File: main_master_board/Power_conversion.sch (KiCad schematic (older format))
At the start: 64 parts, among them IC1 IC_MCP73831, U10 FDS4935A, U11 Si1900DL, U12 FDS4935A, U2 LP3852-3.3, U20 TPS82084SIL, U3 TPS61232DRC, U4 LMR16030, U5 Si1900DL, U6 74AUC1G32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

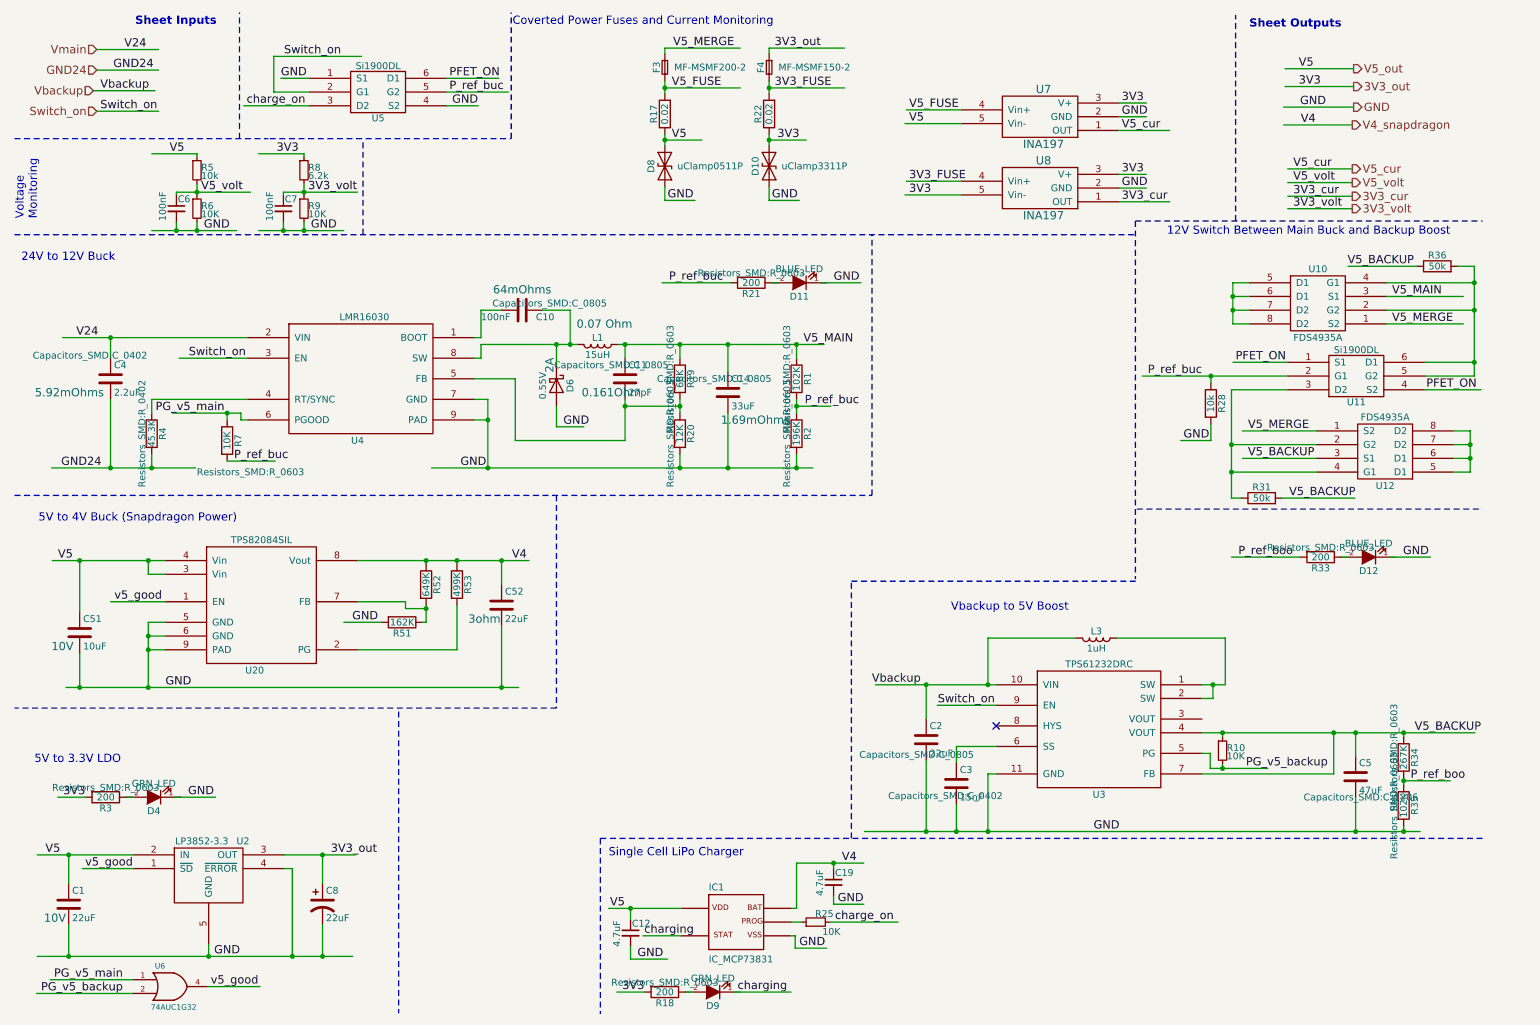
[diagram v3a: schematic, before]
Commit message: Cleaned up some wires and moved connectors out to main page. Also added some LEDs
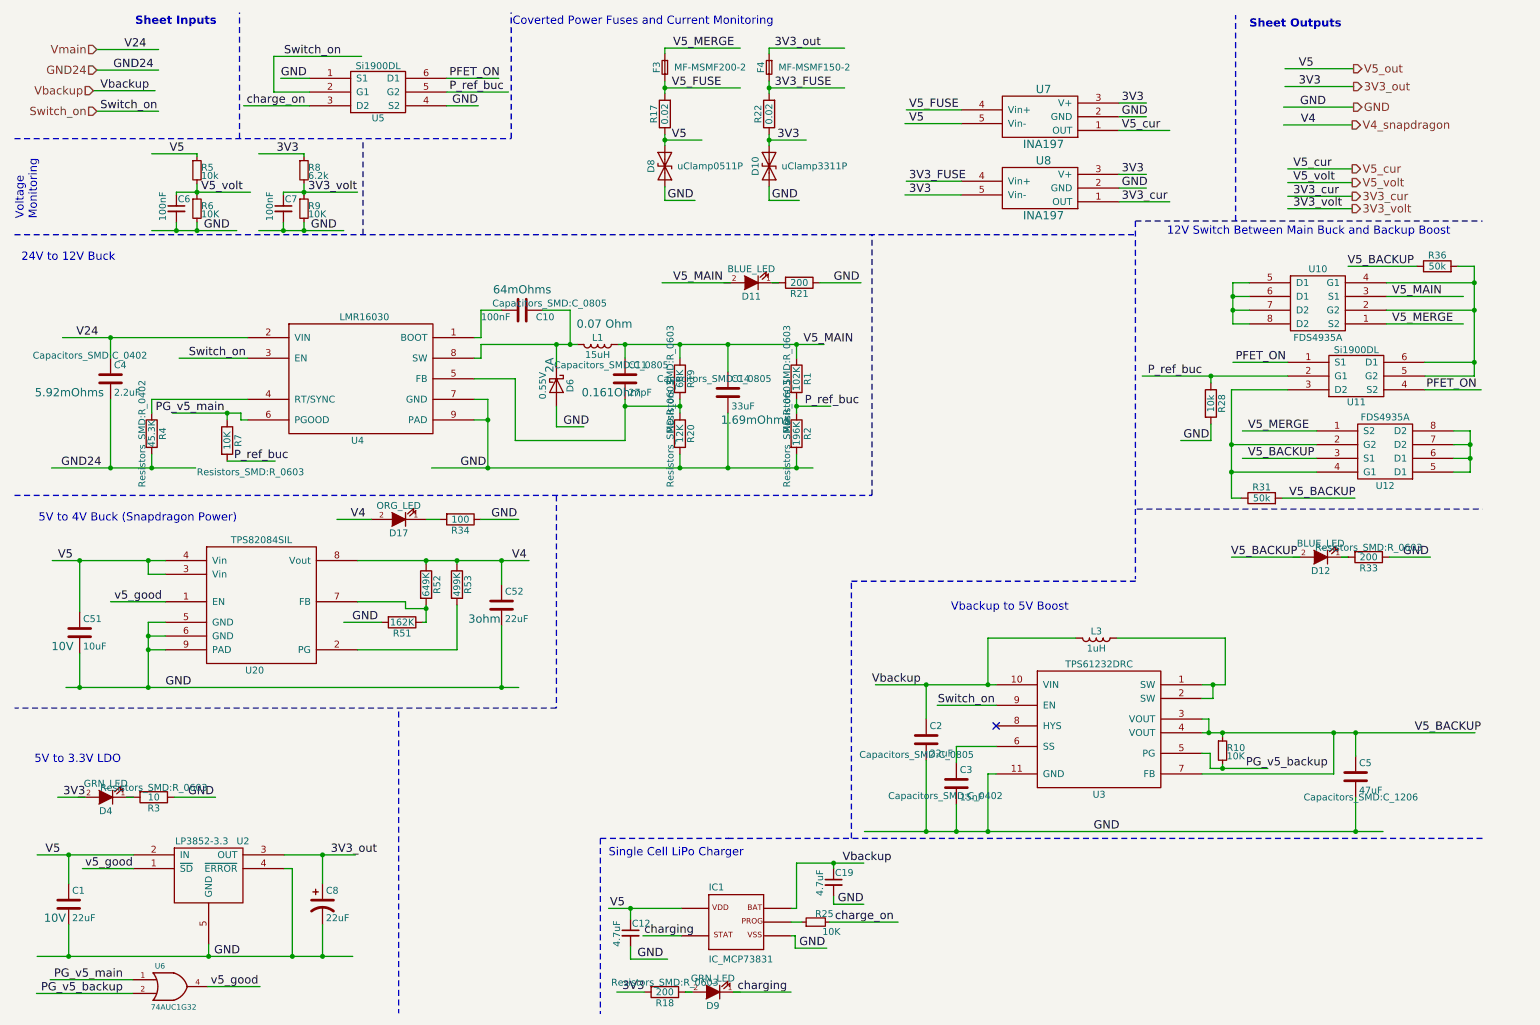
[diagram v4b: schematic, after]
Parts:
- removed R35: 102K, Resistors_SMD:R_0603, symbol R
- added D17: ORG_LED, LEDs:LED_0603, symbol LED
- R3: value 200 -> 10
- R34: value 267K -> 100
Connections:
- net labels removed: P_ref_boo
- wire segments 236 -> 237
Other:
- moved on the sheet: D11, D12, D4, R21, R3, R33
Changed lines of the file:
@@
 LIBS:Sensors
 LIBS:LP3852-3.3
-LIBS:decaWave
+LIBS:0s102011ma1qn1
+LIBS:74LVC1G17
+LIBS:74V1T126
+LIBS:acs711klctr-12ab-t
+LIBS:AD7192
+LIBS:AD7193
+LIBS:am-hrr30-xxx
+LIBS:aon7528
+LIBS:AP7363
+LIBS:AS1359
+LIBS:csd16323q3
+LIBS:dmn2004dmk
+LIBS:dp_devices
+LIBS:DSPIC33E128MC506
+LIBS:fds6898az
+LIBS:ina197
+LIBS:irf7329pbf
+LIBS:ld1117
+LIBS:lm3478
+LIBS:lm3481
+LIBS:lt1910
+LIBS:ltc1871
+LIBS:ltc1982
+LIBS:MAG3110
+LIBS:mcp1700
+LIBS:mcp73831
+LIBS:mcsmt-g5030a1-3712
+LIBS:microchip_can
+LIBS:microclasp_hdrx2
+LIBS:microclasp_hdrx3
+LIBS:MPU-6000_MPU-6050
+LIBS:MPU-9150
+LIBS:nrf24l01+
+LIBS:pds1040l
+LIBS:pic12f1571
+LIBS:pinhead
+LIBS:psmn013-80ys
+LIBS:RESISTOR_ARRAY
+LIBS:rf803d
+LIBS:RGB_LED
+LIBS:Si1970DH
+LIBS:sn65hvd232
+LIBS:ssc54
+LIBS:sw_push_4
+LIBS:tc74
+LIBS:TPS2113A
+LIBS:tps54540
+LIBS:vs-mbrb1635pbf
+LIBS:xal5050-562meb
+LIBS:xal6030-182mec
 LIBS:conn_2x50
 LIBS:conn_open_q_x2
@@
 LIBS:ac-dc
 LIBS:actel
-LIBS:allegro
 LIBS:Altera
 LIBS:analog_devices
@@
 LIBS:logo
 LIBS:maxim
-LIBS:mechanical
 LIBS:microchip_dspic33dsc
 LIBS:microchip_pic10mcu
@@
 LIBS:microchip_pic32mcu
 LIBS:motor_drivers
-LIBS:motors
 LIBS:msp430
 LIBS:nordicsemi
@@
 LIBS:ttl_ieee
 LIBS:video
-LIBS:wiznet
 LIBS:Worldsemi
 LIBS:Xicor
-LIBS:zetex
 LIBS:Zilog
 LIBS:conn_2x45
@@
 $Descr A4 11693 8268
 encoding utf-8
-Sheet 2 7
+Sheet 2 6
 Title ""
 Date ""
@@
 L R R33
 U 1 1 58669BFA
-P 10020 4450
-F 0 "R33" V 10100 4450 50  0000 C CNN
-F 1 "200" V 10020 4450 50  0000 C CNN
-F 2 "Resistors_SMD:R_0603" V 9950 4450 50  0000 C CNN
-F 3 "" H 10020 4450 50  0000 C CNN
-	1    10020 4450
+P 10370 4450
+F 0 "R33" V 10450 4450 50  0000 C CNN
+F 1 "200" V 10370 4450 50  0000 C CNN
+F 2 "Resistors_SMD:R_0603" V 10300 4450 50  0000 C CNN
+F 3 "" H 10370 4450 50  0000 C CNN
+	1    10370 4450
 	0    1    1    0
 $EndComp
@@
 L LED-RESCUE-main_master_board D?
 U 1 1 5866D243
-P 1515 6200
+P 1165 6200
 AR Path="/5866D243" Ref="D?"  Part="1"
 AR Path="/58643B62/5866D243" Ref="D4"  Part="1"
 AR Path="/5876FF98/5866D243" Ref="D4"  Part="1"
-F 0 "D4" H 1515 6300 50  0000 C CNN
-F 1 "GRN_LED" H 1515 6100 50  0000 C CNN
-F 2 "LEDs:LED_0603" H 1515 6200 50  0001 C CNN
-F 3 "http://www.digikey.com/product-detail/en/kingbright/APT1608ZGC/754-1126-1-ND" H 1515 6200 50  0001 C CNN
-	1    1515 6200
+F 0 "D4" H 1165 6300 50  0000 C CNN
+F 1 "GRN_LED" H 1165 6100 50  0000 C CNN
+F 2 "LEDs:LED_0603" H 1165 6200 50  0001 C CNN
+F 3 "http://www.digikey.com/product-detail/en/kingbright/APT1608ZGC/754-1126-1-ND" H 1165 6200 50  0001 C CNN
+	1    1165 6200
 	-1   0    0    1
 $EndComp
@@
 L R R3
 U 1 1 5866D24A
-P 1165 6200
-F 0 "R3" V 1245 6200 50  0000 C CNN
-F 1 "200" V 1165 6200 50  0000 C CNN
-F 2 "Resistors_SMD:R_0603" V 1095 6200 50  0000 C CNN
-F 3 "" H 1165 6200 50  0000 C CNN
-	1    1165 6200
+P 1515 6200
+F 0 "R3" V 1595 6200 50  0000 C CNN
+F 1 "10" V 1515 6200 50  0000 C CNN
+F 2 "Resistors_SMD:R_0603" V 1445 6200 50  0000 C CNN
+F 3 "" H 1515 6200 50  0000 C CNN
+	1    1515 6200
 	0    1    1    0
 $EndComp
@@
 Vbackup
 $Comp
-L R R34
-U 1 1 586BFF78
-P 10625 5910
-F 0 "R34" V 10705 5910 50  0000 C CNN
-F 1 "267K" V 10625 5910 50  0000 C CNN
-F 2 "Resistors_SMD:R_0603" V 10555 5910 50  0000 C CNN
-F 3 "" H 10625 5910 50  0000 C CNN
-	1    10625 5910
-	1    0    0    -1
-$EndComp
-$Comp
-L R R35
-U 1 1 586C095E
-P 10625 6260
-F 0 "R35" V 10705 6260 50  0000 C CNN
-F 1 "102K" V 10625 6260 50  0000 C CNN
-F 2 "Resistors_SMD:R_0603" V 10555 6260 50  0000 C CNN
-F 3 "" H 10625 6260 50  0000 C CNN
-	1    10625 6260
-	1    0    0    -1
-$EndComp
-Text Label 10675 6080 0    60   ~ 0
-P_ref_boo
-Text Label 9420 4450 0    60   ~ 0
-P_ref_boo
-$Comp
 L LED-RESCUE-main_master_board D11
 U 1 1 586C4FFA
-P 6220 2450
-F 0 "D11" H 6220 2550 50  0000 C CNN
-F 1 "BLUE_LED" H 6220 2350 50  0000 C CNN
-F 2 "LEDs:LED_0603" H 6220 2450 50  0001 C CNN
-F 3 "http://www.digikey.com/product-detail/en/vishay-semiconductor-opto-division/VLMB1310-GS08/VLMB1310-GS08CT-ND" H 6220 2450 50  0001 C CNN
-	1    6220 2450
+P 5870 2450
+F 0 "D11" H 5870 2550 50  0000 C CNN
+F 1 "BLUE_LED" H 5870 2350 50  0000 C CNN
+F 2 "LEDs:LED_0603" H 5870 2450 50  0001 C CNN
+F 3 "http://www.digikey.com/product-detail/en/vishay-semiconductor-opto-division/VLMB1310-GS08/VLMB1310-GS08CT-ND" H 5870 2450 50  0001 C CNN
+	1    5870 2450
 	-1   0    0    1
 $EndComp
@@
 L R R21
 U 1 1 586C5001
-P 5870 2450
-F 0 "R21" V 5950 2450 50  0000 C CNN
-F 1 "200" V 5870 2450 50  0000 C CNN
-F 2 "Resistors_SMD:R_0603" V 5800 2450 50  0000 C CNN
-F 3 "" H 5870 2450 50  0000 C CNN
-	1    5870 2450
+P 6220 2450
+F 0 "R21" V 6300 2450 50  0000 C CNN
+F 1 "200" V 6220 2450 50  0000 C CNN
+F 2 "Resistors_SMD:R_0603" V 6150 2450 50  0001 C CNN
+F 3 "" H 6220 2450 50  0000 C CNN
+	1    6220 2450
 	0    1    1    0
 $EndComp
-Text Label 5270 2450 0    60   ~ 0
-P_ref_buc
 Text Label 6260 3350 0    60   ~ 0
 P_ref_buc
@@
 L LED-RESCUE-main_master_board D12
 U 1 1 586C9705
-P 10370 4450
-F 0 "D12" H 10370 4550 50  0000 C CNN
-F 1 "BLUE_LED" H 10370 4350 50  0000 C CNN
-F 2 "LEDs:LED_0603" H 10370 4450 50  0001 C CNN
-F 3 "http://www.digikey.com/product-detail/en/vishay-semiconductor-opto-division/VLMB1310-GS08/VLMB1310-GS08CT-ND" H 10370 4450 50  0001 C CNN
-	1    10370 4450
+P 10020 4450
+F 0 "D12" H 10020 4550 50  0000 C CNN
+F 1 "BLUE_LED" H 10020 4350 50  0000 C CNN
+F 2 "LEDs:LED_0603" H 10020 4450 50  0001 C CNN
+F 3 "http://www.digikey.com/product-detail/en/vishay-semiconductor-opto-division/VLMB1310-GS08/VLMB1310-GS08CT-ND" H 10020 4450 50  0001 C CNN
+	1    10020 4450
 	-1   0    0    1
 $EndComp
@@
 Text Label 9400 3030 0    60   ~ 0
 PFET_ON
-Text Label 8760 3130 0    60   ~ 0
-P_ref_buc
 Text Label 9020 3600 0    60   ~ 0
 GND
@@
 Text Label 6500 6980 0    60   ~ 0
 GND
-Text Label 6530 6680 0    60   ~ 0
-V4
 Text Notes 4830 6640 0    60   ~ 0
 Single Cell LiPo Charger
@@
 	11200 6500 5700 6500
 Wire Wire Line
-	10625 6060 10625 6110
-Wire Wire Line
-	10625 6080 10965 6080
-Connection ~ 10625 6080
-Wire Wire Line
 	5220 2450 5720 2450
 Wire Wire Line
@@
 	10260 1170 9750 1170
 Wire Wire Line
-	6695 6450 10745 6450
+	6695 6450 10475 6450
 Wire Wire Line
 	7655 6030 7595 6030
@@
 Connection ~ 10115 5730
 Wire Wire Line
-	10275 6200 10275 6450
+	10275 6450 10275 6200
 Connection ~ 10275 6450
 Wire Wire Line
@@
 Switch_on
 NoConn ~ 7655 5680
-Wire Wire Line
-	10625 5760 10625 5730
-Connection ~ 10625 5730
-Wire Wire Line
-	10625 6410 10625 6450
-Connection ~ 10625 6450
 Text Label 10705 5730 0    60   ~ 0
 V5_BACKUP
@@
 Text Label 9875 1300 0    60   ~ 0
 V4
+Text Label 5300 2450 0    60   ~ 0
+V5_MAIN
+Text Label 9850 4450 2    60   ~ 0
+V5_BACKUP
+Text Label 6535 6680 0    60   ~ 0
+Vbackup
+$Comp
+L LED D17
+U 1 1 588AAACC
+P 3300 4175
+F 0 "D17" H 3300 4275 50  0000 C CNN
+F 1 "ORG_LED" H 3300 4075 50  0000 C CNN
+F 2 "LEDs:LED_0603" H 3300 4175 50  0001 C CNN
+F 3 "" H 3300 4175 50  0000 C CNN
+	1    3300 4175
+	-1   0    0    1
+$EndComp
+$Comp
+L R R34
+U 1 1 588AB24C
+P 3750 4175
+F 0 "R34" V 3830 4175 50  0000 C CNN
+F 1 "100" V 3750 4175 50  0000 C CNN
+F 2 "Resistors_SMD:R_0603" V 3680 4175 50  0001 C CNN
+F 3 "" H 3750 4175 50  0000 C CNN
+	1    3750 4175
+	0    1    1    0
+$EndComp
+Text Label 3975 4175 0    60   ~ 0
+GND
+Wire Wire Line
+	3900 4175 4175 4175
+Wire Wire Line
+	3500 4175 3600 4175
+Wire Wire Line
+	3100 4175 2850 4175
+Text Label 2950 4175 0    60   ~ 0
+V4
+Wire Wire Line
+	9155 5630 9205 5630
+Wire Wire Line
+	9205 5630 9205 5730
+Connection ~ 9205 5730
+Text Label 8760 3130 0    60   ~ 0
+P_ref_buc
 $EndSCHEMATC

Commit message: Started routing! 24 to 5 buck
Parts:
- D17: symbol LED -> LED-RESCUE-main_master_board
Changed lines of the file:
@@
 LIBS:Sensors
 LIBS:LP3852-3.3
-LIBS:0s102011ma1qn1
-LIBS:74LVC1G17
-LIBS:74V1T126
-LIBS:acs711klctr-12ab-t
-LIBS:AD7192
-LIBS:AD7193
-LIBS:am-hrr30-xxx
-LIBS:aon7528
-LIBS:AP7363
-LIBS:AS1359
-LIBS:csd16323q3
-LIBS:dmn2004dmk
-LIBS:dp_devices
-LIBS:DSPIC33E128MC506
-LIBS:fds6898az
-LIBS:ina197
-LIBS:irf7329pbf
-LIBS:ld1117
-LIBS:lm3478
-LIBS:lm3481
-LIBS:lt1910
-LIBS:ltc1871
-LIBS:ltc1982
-LIBS:MAG3110
-LIBS:mcp1700
-LIBS:mcp73831
-LIBS:mcsmt-g5030a1-3712
-LIBS:microchip_can
-LIBS:microclasp_hdrx2
-LIBS:microclasp_hdrx3
-LIBS:MPU-6000_MPU-6050
-LIBS:MPU-9150
-LIBS:nrf24l01+
-LIBS:pds1040l
-LIBS:pic12f1571
-LIBS:pinhead
-LIBS:psmn013-80ys
-LIBS:RESISTOR_ARRAY
-LIBS:rf803d
-LIBS:RGB_LED
-LIBS:Si1970DH
-LIBS:sn65hvd232
-LIBS:ssc54
-LIBS:sw_push_4
-LIBS:tc74
-LIBS:TPS2113A
-LIBS:tps54540
-LIBS:vs-mbrb1635pbf
-LIBS:xal5050-562meb
-LIBS:xal6030-182mec
+LIBS:decaWave
 LIBS:conn_2x50
 LIBS:conn_open_q_x2
@@
 LIBS:ac-dc
 LIBS:actel
+LIBS:allegro
 LIBS:Altera
 LIBS:analog_devices
@@
 LIBS:logo
 LIBS:maxim
+LIBS:mechanical
 LIBS:microchip_dspic33dsc
 LIBS:microchip_pic10mcu
@@
 LIBS:microchip_pic32mcu
 LIBS:motor_drivers
+LIBS:motors
 LIBS:msp430
 LIBS:nordicsemi
@@
 LIBS:ttl_ieee
 LIBS:video
+LIBS:wiznet
 LIBS:Worldsemi
 LIBS:Xicor
+LIBS:zetex
 LIBS:Zilog
 LIBS:conn_2x45
@@
 F 0 "C14" H 5725 3350 50  0000 L CNN
 F 1 "33uF" H 5725 3150 50  0000 L CNN
-F 2 "Capacitors_SMD:C_0805" H 5600 3350 50  0000 C CNN
+F 2 "Capacitors_SMD:C_0805" H 5600 3300 50  0000 C CNN
 F 3 "" H 5700 3250 50  0000 C CNN
 F 4 "1.69mOhms" H 5900 3050 60  0000 C CNN "Resistance"
@@
 F 1 "LMR16030" H 3050 3600 50  0000 C CNN
 F 2 "HSOIC-8:HSOIC-8-1EP_Pitch1.27mm" H 2650 2700 50  0001 C CNN
-F 3 "DOCUMENTATION" H 3450 2700 50  0001 C CNN
+F 3 "http://www.digikey.com/product-detail/en/LMR16030PDDA/296-44513-5-ND/" H 3450 2700 50  0001 C CNN
 	1    3050 3150
 	1    0    0    -1
@@
 Vbackup
 $Comp
-L LED D17
+L LED-RESCUE-main_master_board D17
 U 1 1 588AAACC
 P 3300 4175
+AR Path="/588AAACC" Ref="D17"  Part="1"
+AR Path="/58643B62/588AAACC" Ref="D17"  Part="1"
 F 0 "D17" H 3300 4275 50  0000 C CNN
 F 1 "ORG_LED" H 3300 4075 50  0000 C CNN

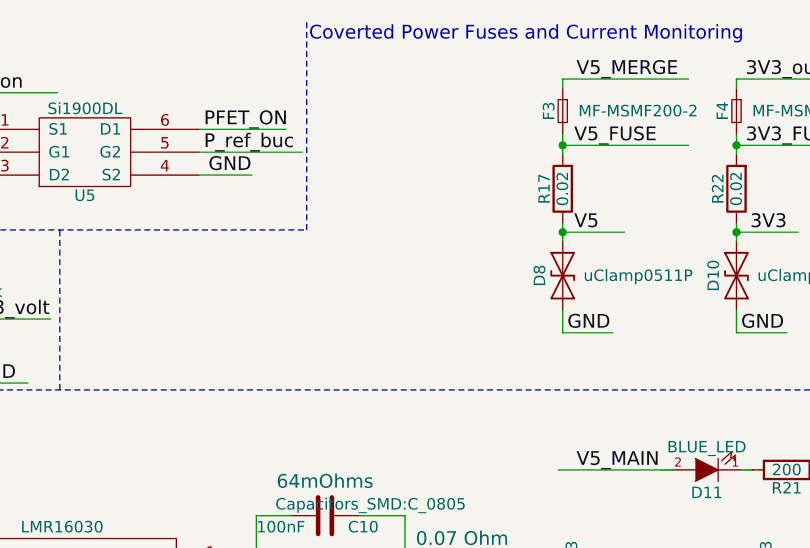
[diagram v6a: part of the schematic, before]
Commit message: Routing power. Added 5V leveling cap.
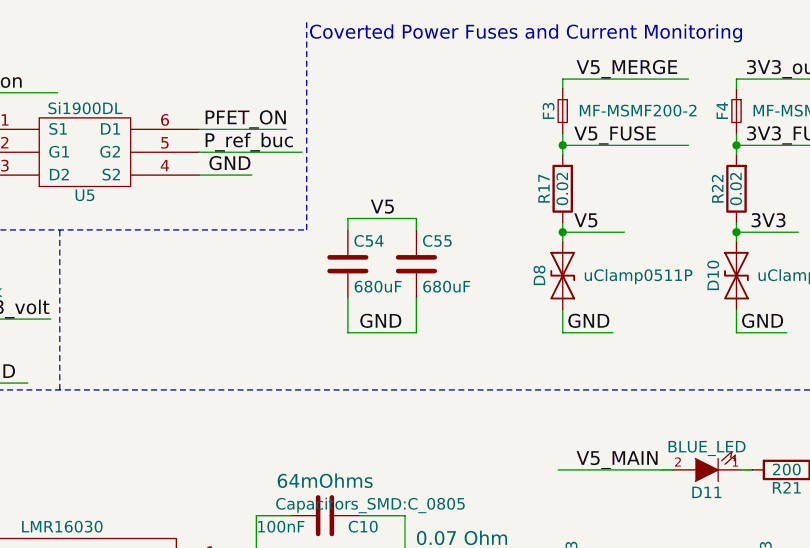
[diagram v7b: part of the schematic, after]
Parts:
- added C54, C55: 680uF, Capacitors_ThroughHole:CP_Radial_D6.3mm_P2.50mm, symbol C
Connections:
- wire segments 237 -> 243
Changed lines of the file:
@@
 $Descr A4 11693 8268
 encoding utf-8
-Sheet 2 6
+Sheet 2 5
 Title ""
 Date ""
@@
 Text Label 8760 3130 0    60   ~ 0
 P_ref_buc
+$Comp
+L C C54
+U 1 1 58933091
+P 4300 1550
+F 0 "C54" H 4325 1650 50  0000 L CNN
+F 1 "680uF" H 4325 1450 50  0000 L CNN
+F 2 "Capacitors_ThroughHole:CP_Radial_D6.3mm_P2.50mm" H 4338 1400 50  0001 C CNN
+F 3 "http://www.digikey.com/product-detail/en/nichicon/UCL1A681MNL1GS/493-3909-1-ND/2300336" H 4300 1550 50  0001 C CNN
+	1    4300 1550
+	1    0    0    -1
+$EndComp
+$Comp
+L C C55
+U 1 1 589344EC
+P 4600 1550
+F 0 "C55" H 4625 1650 50  0000 L CNN
+F 1 "680uF" H 4625 1450 50  0000 L CNN
+F 2 "Capacitors_ThroughHole:CP_Radial_D6.3mm_P2.50mm" H 4638 1400 50  0001 C CNN
+F 3 "http://www.digikey.com/product-detail/en/nichicon/UCL1A681MNL1GS/493-3909-1-ND/2300336" H 4600 1550 50  0001 C CNN
+	1    4600 1550
+	1    0    0    -1
+$EndComp
+Text Label 4400 1350 0    60   ~ 0
+V5
+Wire Wire Line
+	4600 1400 4600 1350
+Wire Wire Line
+	4600 1350 4300 1350
+Wire Wire Line
+	4300 1350 4300 1400
+Wire Wire Line
+	4300 1700 4300 1850
+Wire Wire Line
+	4300 1850 4600 1850
+Wire Wire Line
+	4600 1850 4600 1700
+Text Label 4350 1850 0    60   ~ 0
+GND
 $EndSCHEMATC
